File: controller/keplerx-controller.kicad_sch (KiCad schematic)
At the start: 21 parts, among them J1 Conn_02x05_Odd_Even, J2 Conn_01x04, J3 Conn_01x04, SW1 Synth, SW2 ROM, SW3 Vol-, SW4 Vol+, SW5 RotaryEncoder_Switch

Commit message: 再再度出し直し(v2.0.2)
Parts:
- added H5, H6, H7, H8: MountingHole_Pad, MountingHole:MountingHole_2.2mm_M2_ISO7380_Pad, symbol Mechanical:MountingHole_Pad
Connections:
- net GND: now also H5.1, H6.1, H7.1, H8.1
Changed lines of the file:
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@@
   (junction (at 203.835 109.22) (diameter 0) (color 0 0 0 0)
   )
+  (junction (at 254 109.22) (diameter 0) (color 0 0 0 0)
+  )
   (junction (at 173.99 73.025) (diameter 0) (color 0 0 0 0)
   )
@@
   (junction (at 90.17 109.22) (diameter 0) (color 0 0 0 0)
   )
+  (junction (at 245.745 109.22) (diameter 0) (color 0 0 0 0)
+  )
   (junction (at 210.82 73.025) (diameter 0) (color 0 0 0 0)
   )
+  (junction (at 237.49 109.22) (diameter 0) (color 0 0 0 0)
+  )
   (junction (at 163.195 109.22) (diameter 0) (color 0 0 0 0)
   )
   (junction (at 207.01 89.535) (diameter 0) (color 0 0 0 0)
   )
+  (junction (at 213.36 109.22) (diameter 0) (color 0 0 0 0)
+  )
   (junction (at 210.82 50.8) (diameter 0) (color 0 0 0 0)
   )
@@
     (stroke (width 0) (type default) (color 0 0 0 0))
   )
+  (wire (pts (xy 237.49 109.22) (xy 213.36 109.22))
+    (stroke (width 0) (type default) (color 0 0 0 0))
+  )
+  (wire (pts (xy 263.525 106.68) (xy 263.525 109.22))
+    (stroke (width 0) (type default) (color 0 0 0 0))
+  )
   (wire (pts (xy 203.835 109.22) (xy 195.58 109.22))
     (stroke (width 0) (type default) (color 0 0 0 0))
@@
     (stroke (width 0) (type default) (color 0 0 0 0))
   )
+  (wire (pts (xy 263.525 109.22) (xy 254 109.22))
+    (stroke (width 0) (type default) (color 0 0 0 0))
+  )
+  (wire (pts (xy 245.745 106.68) (xy 245.745 109.22))
+    (stroke (width 0) (type default) (color 0 0 0 0))
+  )
   (wire (pts (xy 195.58 109.22) (xy 187.325 109.22))
     (stroke (width 0) (type default) (color 0 0 0 0))
@@
     (stroke (width 0) (type default) (color 0 0 0 0))
   )
+  (wire (pts (xy 166.37 118.11) (xy 166.37 121.285))
+    (stroke (width 0) (type default) (color 0 0 0 0))
+  )
+  (wire (pts (xy 254 109.22) (xy 245.745 109.22))
+    (stroke (width 0) (type default) (color 0 0 0 0))
+  )
   (wire (pts (xy 210.82 89.535) (xy 207.01 89.535))
     (stroke (width 0) (type default) (color 0 0 0 0))
@@
     (stroke (width 0) (type default) (color 0 0 0 0))
   )
+  (wire (pts (xy 245.745 109.22) (xy 237.49 109.22))
+    (stroke (width 0) (type default) (color 0 0 0 0))
+  )
   (wire (pts (xy 78.74 70.485) (xy 77.47 70.485))
     (stroke (width 0) (type default) (color 0 0 0 0))
@@
     (stroke (width 0) (type default) (color 0 0 0 0))
   )
+  (wire (pts (xy 254 106.68) (xy 254 109.22))
+    (stroke (width 0) (type default) (color 0 0 0 0))
+  )
   (wire (pts (xy 213.36 106.68) (xy 213.36 109.22))
     (stroke (width 0) (type default) (color 0 0 0 0))
@@
   )
   (wire (pts (xy 195.58 106.68) (xy 195.58 109.22))
+    (stroke (width 0) (type default) (color 0 0 0 0))
+  )
+  (wire (pts (xy 237.49 106.68) (xy 237.49 109.22))
     (stroke (width 0) (type default) (color 0 0 0 0))
   )
@@
     (pin "S2")
   )
+  (symbol (lib_id "Mechanical:MountingHole_Pad") (at 245.745 104.14 0) (unit 1)
+    (in_bom yes) (on_board yes)
+    (property "Reference" "H6" (id 0) (at 248.92 101.5999 0)
+      (effects (font (size 1.27 1.27)) (justify left))
+    )
+    (property "Value" "MountingHole_Pad" (id 1) (at 248.92 104.1399 0)
+      (effects (font (size 1.27 1.27)) (justify left))
+    )
+    (property "Footprint" "MountingHole:MountingHole_2.2mm_M2_ISO7380_Pad" (id 2) (at 245.745 104.14 0)
+      (effects (font (size 1.27 1.27)) hide)
+    )
+    (property "Datasheet" "~" (id 3) (at 245.745 104.14 0)
+      (effects (font (size 1.27 1.27)) hide)
+    )
+    (pin "1")
+  )
   (symbol (lib_id "Device:C_Polarized_Small_US") (at 173.99 46.99 0) (unit 1)
     (in_bom yes) (on_board yes) (fields_autoplaced)
@@
     (pin "2")
   )
+  (symbol (lib_id "Mechanical:MountingHole_Pad") (at 237.49 104.14 0) (unit 1)
+    (in_bom yes) (on_board yes)
+    (property "Reference" "H5" (id 0) (at 240.665 101.5999 0)
+      (effects (font (size 1.27 1.27)) (justify left))
+    )
+    (property "Value" "MountingHole_Pad" (id 1) (at 240.665 104.1399 0)
+      (effects (font (size 1.27 1.27)) (justify left))
+    )
+    (property "Footprint" "MountingHole:MountingHole_2.2mm_M2_ISO7380_Pad" (id 2) (at 237.49 104.14 0)
+      (effects (font (size 1.27 1.27)) hide)
+    )
+    (property "Datasheet" "~" (id 3) (at 237.49 104.14 0)
+      (effects (font (size 1.27 1.27)) hide)
+    )
+    (pin "1")
+  )
   (symbol (lib_id "Mechanical:MountingHole_Pad") (at 213.36 104.14 0) (unit 1)
     (in_bom yes) (on_board yes)
@@
     (pin "3")
     (pin "4")
+  )
+  (symbol (lib_id "power:GND") (at 166.37 121.285 0) (unit 1)
+    (in_bom yes) (on_board yes) (fields_autoplaced)
+    (property "Reference" "#PWR02" (id 0) (at 166.37 127.635 0)
+      (effects (font (size 1.27 1.27)) hide)
+    )
+    (property "Value" "GND" (id 1) (at 166.37 125.73 0))
+    (property "Footprint" "" (id 2) (at 166.37 121.285 0)
+      (effects (font (size 1.27 1.27)) hide)
+    )
+    (property "Datasheet" "" (id 3) (at 166.37 121.285 0)
+      (effects (font (size 1.27 1.27)) hide)
+    )
+    (pin "1")
   )
   (symbol (lib_id "Jumper:Jumper_2_Open") (at 214.63 57.15 270) (unit 1)
@@
     (pin "9")
   )
+  (symbol (lib_id "Mechanical:MountingHole_Pad") (at 263.525 104.14 0) (unit 1)
+    (in_bom yes) (on_board yes)
+    (property "Reference" "H8" (id 0) (at 266.7 101.5999 0)
+      (effects (font (size 1.27 1.27)) (justify left))
+    )
+    (property "Value" "MountingHole_Pad" (id 1) (at 266.7 104.1399 0)
+      (effects (font (size 1.27 1.27)) (justify left))
+    )
+    (property "Footprint" "MountingHole:MountingHole_2.2mm_M2_ISO7380_Pad" (id 2) (at 263.525 104.14 0)
+      (effects (font (size 1.27 1.27)) hide)
+    )
+    (property "Datasheet" "~" (id 3) (at 263.525 104.14 0)
+      (effects (font (size 1.27 1.27)) hide)
+    )
+    (pin "1")
+  )
   (symbol (lib_id "Switch:SW_Push") (at 109.22 65.405 0) (unit 1)
     (in_bom yes) (on_board yes) (fields_autoplaced)
@@
     (pin "2")
   )
+  (symbol (lib_id "Mechanical:MountingHole_Pad") (at 254 104.14 0) (unit 1)
+    (in_bom yes) (on_board yes)
+    (property "Reference" "H7" (id 0) (at 257.175 101.5999 0)
+      (effects (font (size 1.27 1.27)) (justify left))
+    )
+    (property "Value" "MountingHole_Pad" (id 1) (at 257.175 104.1399 0)
+      (effects (font (size 1.27 1.27)) (justify left))
+    )
+    (property "Footprint" "MountingHole:MountingHole_2.2mm_M2_ISO7380_Pad" (id 2) (at 254 104.14 0)
+      (effects (font (size 1.27 1.27)) hide)
+    )
+    (property "Datasheet" "~" (id 3) (at 254 104.14 0)
+      (effects (font (size 1.27 1.27)) hide)
+    )
+    (pin "1")
+  )
   (symbol (lib_id "Connector:TestPoint") (at 166.37 34.925 0) (unit 1)
     (in_bom yes) (on_board yes) (fields_autoplaced)
@@
     (pin "1")
     (pin "2")
+  )
+  (symbol (lib_id "power:PWR_FLAG") (at 166.37 118.11 0) (unit 1)
+    (in_bom yes) (on_board yes) (fields_autoplaced)
+    (property "Reference" "#FLG01" (id 0) (at 166.37 116.205 0)
+      (effects (font (size 1.27 1.27)) hide)
+    )
+    (property "Value" "PWR_FLAG" (id 1) (at 166.37 113.03 0))
+    (property "Footprint" "" (id 2) (at 166.37 118.11 0)
+      (effects (font (size 1.27 1.27)) hide)
+    )
+    (property "Datasheet" "~" (id 3) (at 166.37 118.11 0)
+      (effects (font (size 1.27 1.27)) hide)
+    )
+    (pin "1")
   )
   (symbol (lib_id "Switch:SW_Push") (at 121.285 62.865 0) (unit 1)
@@
   )
   (symbol_instances
+    (path "/f434720e-99d4-4765-86bc-91177ee3c881"
+      (reference "#FLG01") (unit 1) (value "PWR_FLAG") (footprint "")
+    )
     (path "/e23ef214-dd4d-40ac-9e93-84538d6d1529"
       (reference "#PWR01") (unit 1) (value "GND") (footprint "")
     )
+    (path "/a002dabd-1b32-48c1-9372-9c1b1eef88ba"
+      (reference "#PWR02") (unit 1) (value "GND") (footprint "")
+    )
     (path "/4ce1be5a-b6cb-4c09-b593-48fe6e835fae"
       (reference "C1") (unit 1) (value "10uF") (footprint "Capacitor_Tantalum_SMD:CP_EIA-3216-10_Kemet-I")
@@
       (reference "H4") (unit 1) (value "MountingHole_Pad") (footprint "MountingHole:MountingHole_3.2mm_M3_Pad")
     )
+    (path "/7deb752a-830f-4d3a-8685-2b7d2cdc9019"
+      (reference "H5") (unit 1) (value "MountingHole_Pad") (footprint "MountingHole:MountingHole_2.2mm_M2_ISO7380_Pad")
+    )
+    (path "/4c9252af-7091-4479-8b63-c2be37714bae"
+      (reference "H6") (unit 1) (value "MountingHole_Pad") (footprint "MountingHole:MountingHole_2.2mm_M2_ISO7380_Pad")
+    )
+    (path "/c11289a1-c022-4e56-ac10-a95c7af4c0fe"
+      (reference "H7") (unit 1) (value "MountingHole_Pad") (footprint "MountingHole:MountingHole_2.2mm_M2_ISO7380_Pad")
+    )
+    (path "/aab3a91a-2f1d-487a-8d69-1d2fd69c320d"
+      (reference "H8") (unit 1) (value "MountingHole_Pad") (footprint "MountingHole:MountingHole_2.2mm_M2_ISO7380_Pad")
+    )
     (path "/a73767b2-8785-4dc6-a8c3-aa4ef02ff8a0"

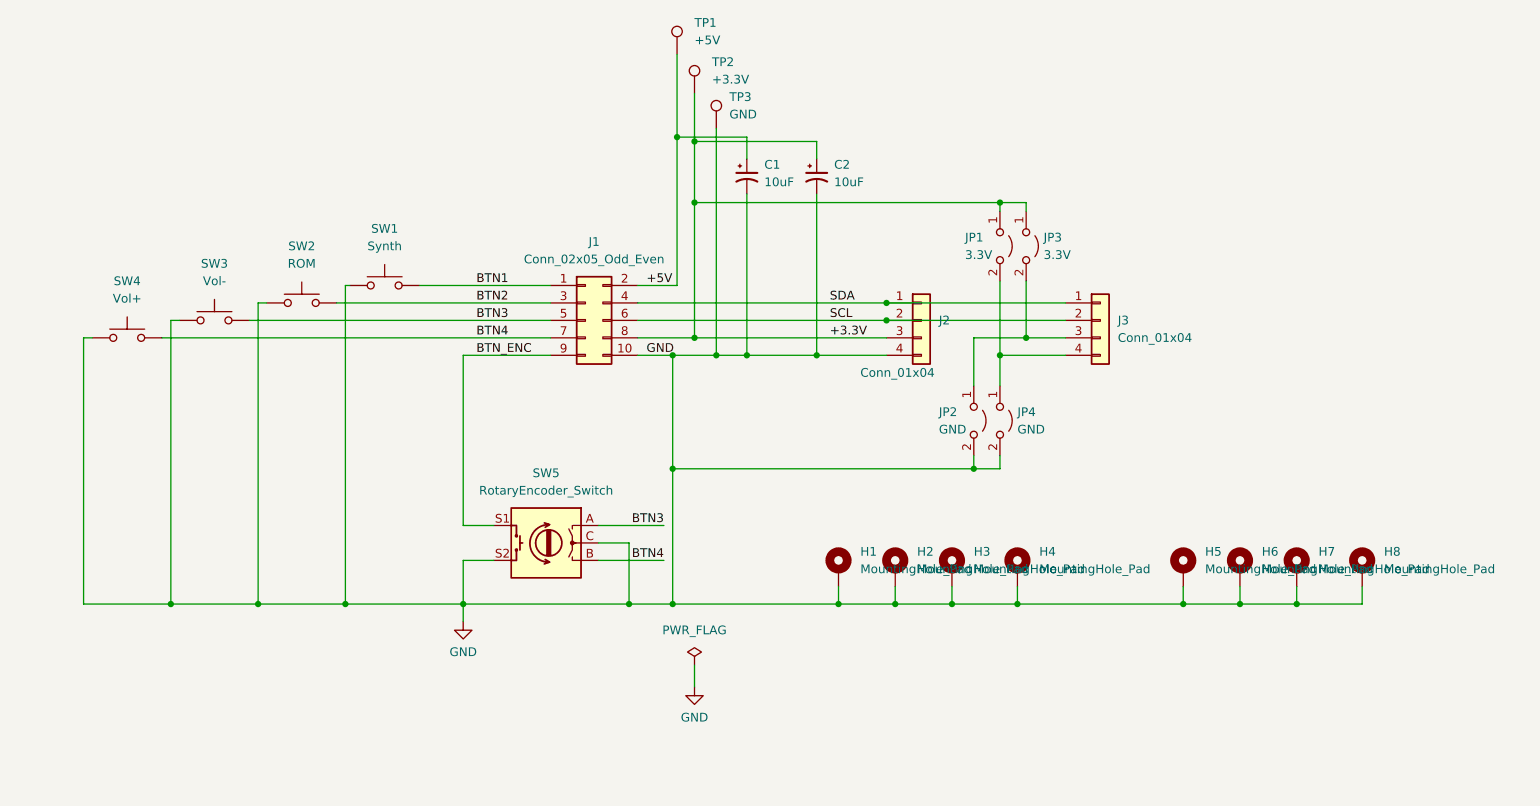
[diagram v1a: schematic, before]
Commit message: v1.0.1 - Changed one of the two sets of open jumper pairs to a bridged jumper
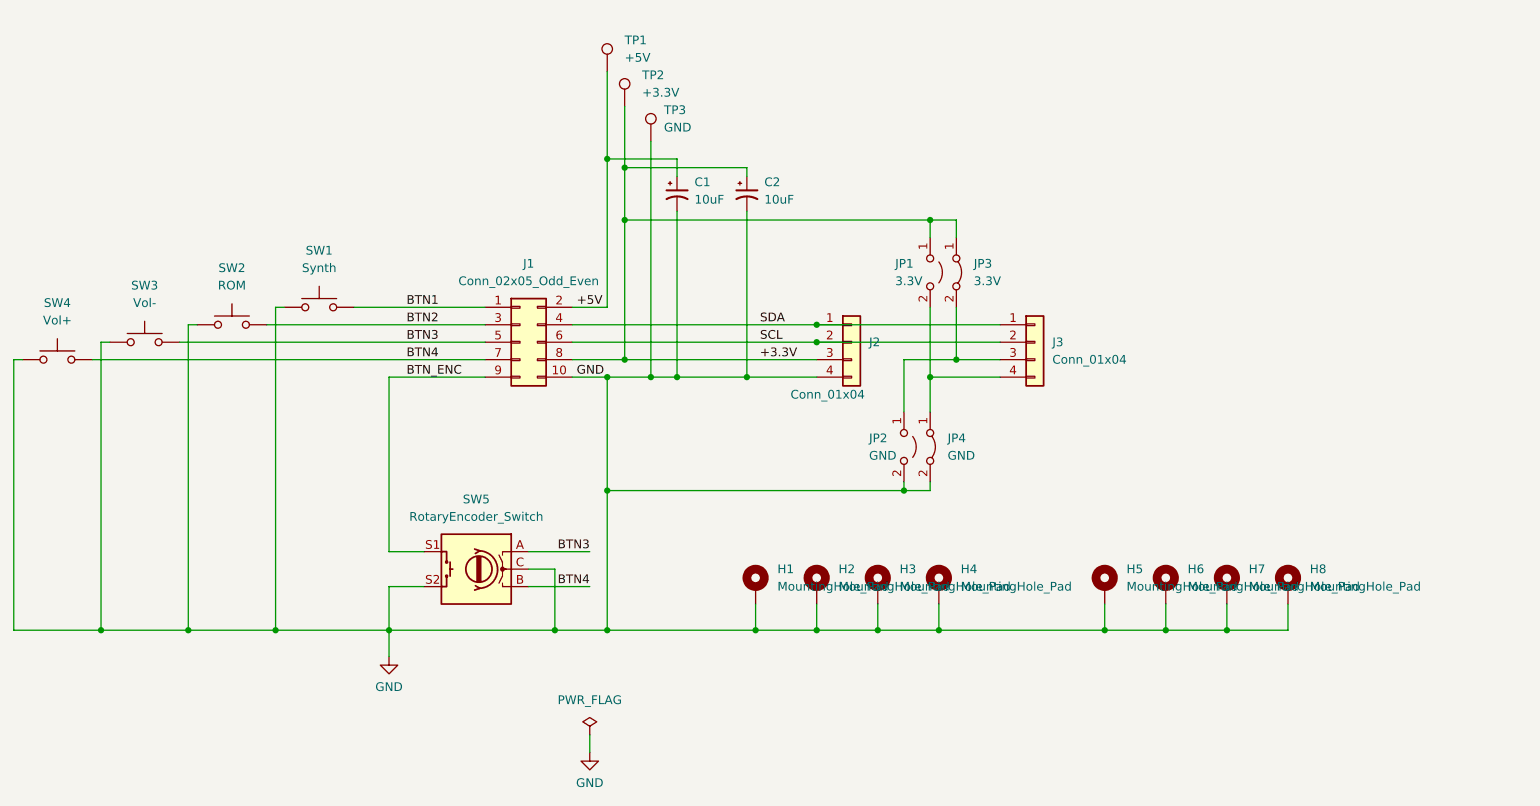
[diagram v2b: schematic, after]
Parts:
- JP3, JP4: footprint Jumper:SolderJumper-2_P1.3mm_Open_RoundedPad1.0x1.5mm -> Jumper:SolderJumper-2_P1.3mm_Bridged2Bar_RoundedPad1.0x1.5mm; symbol Jumper:Jumper_2_Open -> Jumper:Jumper_2_Bridged
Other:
- moved on the sheet: C1, C2, H1, H2, H3, H4, H5, H6, H7, H8, J1, J2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
